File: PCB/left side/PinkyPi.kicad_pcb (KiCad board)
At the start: 2 copper layers, 181.3 x 148.9 mm, 25 parts, among them U5 Pico

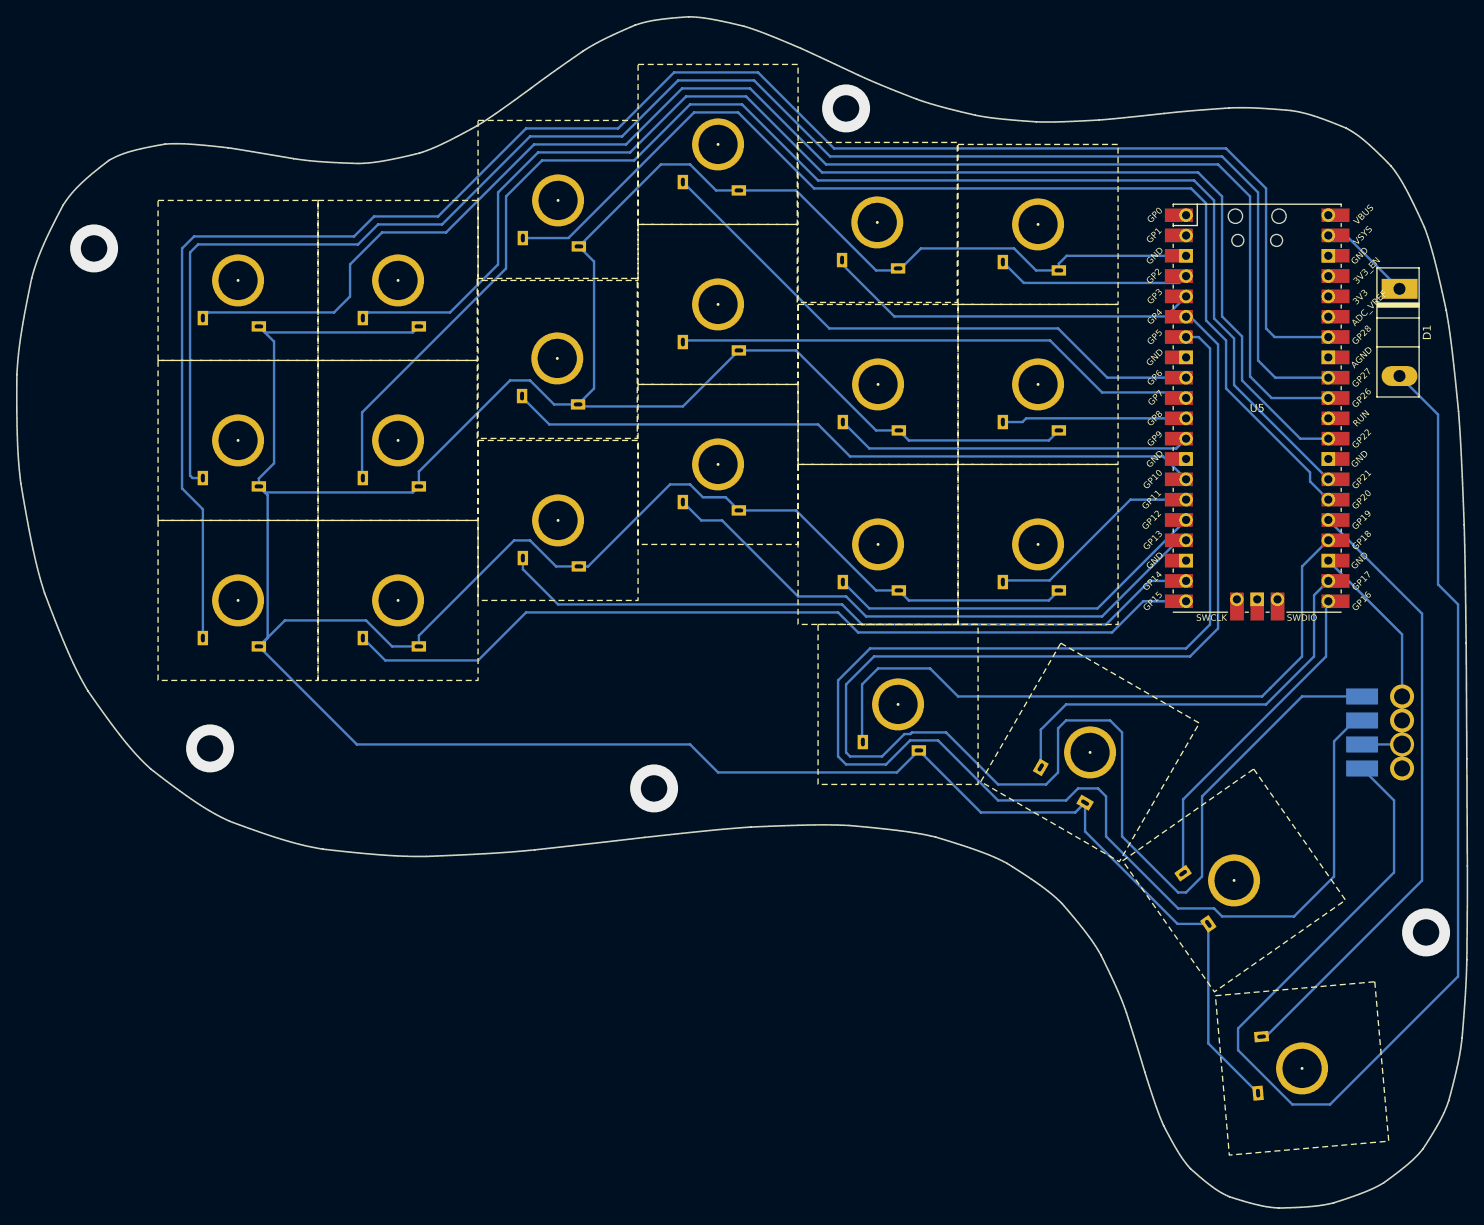
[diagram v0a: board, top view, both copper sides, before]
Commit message: own communication protocol working
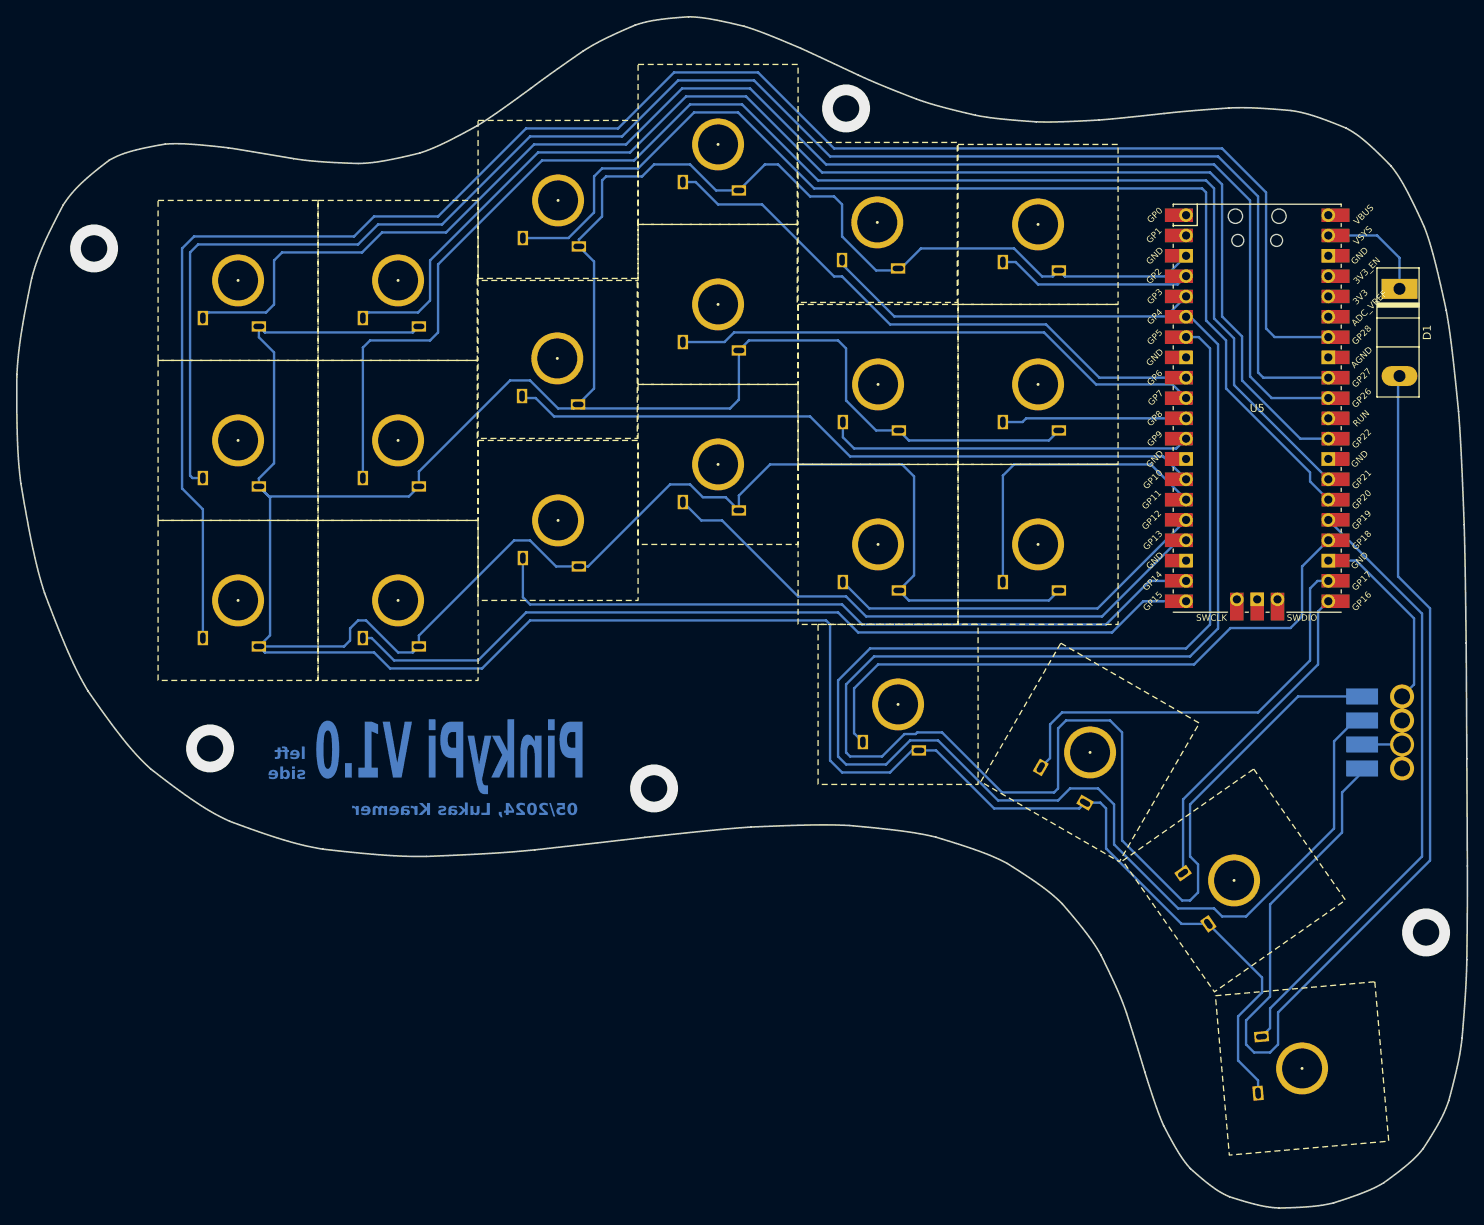
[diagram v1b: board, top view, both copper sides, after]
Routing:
- net GND: track 608.1 -> 666.3 mm
- net Net-(D1-A): track 160.0 -> 138.5 mm
- net /L9: track 27.2 -> 38.6 mm
- net /L19: track 181.7 -> 187.0 mm
- net Net-(U23-TX): track 206.5 -> 211.7 mm
- net /L16: track 82.5 -> 77.8 mm
- net Net-(U23-RX): track 198.1 -> 194.6 mm
- net /L18: track 140.0 -> 143.4 mm
- net Net-(D1-K): track 11.7 -> 13.9 mm
- net /L13: track 89.4 -> 91.5 mm
- net /L20: track 167.2 -> 165.7 mm
- net /L6: track 44.8 -> 45.9 mm
- net /L4: track 66.0 -> 66.8 mm
- net /L7: track 208.5 -> 209.1 mm
- net /L21: track 184.1 -> 184.7 mm
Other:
- board text added: "05/2024, Lukas Kraemer"
- board text added: "PinkyPi V1.0"
- board text added: "left"
- board text added: "side"
